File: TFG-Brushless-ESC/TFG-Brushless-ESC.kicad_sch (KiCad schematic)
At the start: 70 parts, among them J1 V, J2 USB C Receptacle, J3 HALL SENSORS, J4 SWD-I2C, J5 24V IN, J6 U, J7 W, SW1 BOOT0, SW2 NRST, U1 LM317L_SOT-89, U2 LM317, U3 STM32F411CEUx, Y1 25MHz, Y2 32.768kHz

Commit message: PCB v3
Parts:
- D8: value FERD30H100SB -> STPS30100ST; footprint Package_TO_SOT_SMD:TO-252-2 -> Package_TO_SOT_THT:TO-220-3_Vertical
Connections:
- net 24V in: now also J5.1 (Pin_1); no longer J5.2 (Pin_2)
- net GND: now also J5.2 (Pin_2); no longer J5.1 (Pin_1)
- net PA10: no longer D4.1, J3.4 (Pin_4), R15.1
- net PA8: no longer D3.1, J3.2 (Pin_2), R13.1
- net PA9: no longer D3.2, J3.3 (Pin_3), R14.1
- net PB3: now also D3.1, J3.2 (Pin_2), R13.1
- net PB4: now also D3.2, J3.3 (Pin_3), R14.1
- net PB5: now also D4.1, J3.4 (Pin_4), R15.1
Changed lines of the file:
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@@
 		)
 	)
-	(label "PB10"
+	(label "PA9"
 		(at 203.2 78.105 0)
 		(effects
@@
 		)
 	)
-	(label "PA9"
+	(label "PB4"
 		(at 232.41 128.27 0)
 		(effects
@@
 		)
 	)
-	(label "PA3"
+	(label "PA4"
 		(at 203.2 99.06 0)
 		(effects
@@
 		)
 	)
-	(label "PB0"
+	(label "PB1"
 		(at 203.2 85.725 0)
 		(effects
@@
 		)
 	)
-	(label "PA4"
+	(label "PA5"
 		(at 203.2 101.6 0)
 		(effects
@@
 		)
 	)
-	(label "PA10"
+	(label "PB5"
 		(at 232.41 125.73 0)
 		(effects
@@
 		)
 	)
-	(label "PA5"
+	(label "PA6"
 		(at 203.2 96.52 0)
 		(effects
@@
 		)
 	)
-	(label "PA6"
+	(label "PA7"
 		(at 203.2 93.98 0)
 		(effects
@@
 		)
 	)
-	(label "PB1"
+	(label "PA8"
 		(at 203.2 80.645 0)
 		(effects
@@
 		)
 	)
-	(label "PB7"
+	(label "PA3"
 		(at 203.2 109.855 0)
 		(effects
@@
 		)
 	)
-	(label "PA7"
+	(label "PB0"
 		(at 203.2 83.185 0)
 		(effects
@@
 		)
 	)
-	(label "PA8"
+	(label "PB3"
 		(at 232.41 130.81 0)
 		(effects
@@
 		)
 	)
-	(label "PB6"
+	(label "PA2"
 		(at 203.2 112.395 0)
 		(effects
@@
 	)
 	(symbol
-		(lib_id "Connector_Generic:Conn_01x02")
-		(at 56.515 184.15 180)
-		(unit 1)
-		(exclude_from_sim no)
-		(in_bom yes)
-		(on_board yes)
-		(dnp no)
-		(property "Reference" "J5"
-			(at 53.975 184.15 0)
-			(effects
-				(font
-					(size 1.27 1.27)
-				)
-				(justify left)
-			)
-		)
-		(property "Value" "24V IN"
-			(at 53.975 181.61 0)
-			(effects
-				(font
-					(size 1.27 1.27)
-				)
-				(justify left)
-			)
-		)
-		(property "Footprint" "TerminalBlock_Phoenix:TerminalBlock_Phoenix_MKDS-1,5-2-5.08_1x02_P5.08mm_Horizontal"
-			(at 56.515 184.15 0)
-			(effects
-				(font
-					(size 1.27 1.27)
-				)
-				(hide yes)
-			)
-		)
-		(property "Datasheet" "~"
-			(at 56.515 184.15 0)
-			(effects
-				(font
-					(size 1.27 1.27)
-				)
-				(hide yes)
-			)
-		)
-		(property "Description" "Generic connector, single row, 01x02, script generated (kicad-library-utils/schlib/autogen/connector/)"
-			(at 56.515 184.15 0)
-			(effects
-				(font
-					(size 1.27 1.27)
-				)
-				(hide yes)
-			)
-		)
-		(pin "2"
-		)
-		(pin "1"
-		)
-		(instances
-			(project ""
-				(path "/fc8dd9a9-f99a-4338-8182-2c8b4b8ed6dd"
-					(reference "J5")
-					(unit 1)
-				)
-			)
-		)
-	)
-	(symbol
 		(lib_id "Device:D_TVS")
 		(at 119.38 31.115 90)
@@
 	)
 	(symbol
+		(lib_id "Connector_Generic:Conn_01x02")
+		(at 56.515 181.61 0)
+		(mirror y)
+		(unit 1)
+		(exclude_from_sim no)
+		(in_bom yes)
+		(on_board yes)
+		(dnp no)
+		(property "Reference" "J5"
+			(at 53.975 181.61 0)
+			(effects
+				(font
+					(size 1.27 1.27)
+				)
+				(justify left)
+			)
+		)
+		(property "Value" "24V IN"
+			(at 53.975 184.15 0)
+			(effects
+				(font
+					(size 1.27 1.27)
+				)
+				(justify left)
+			)
+		)
+		(property "Footprint" "TerminalBlock_Phoenix:TerminalBlock_Phoenix_MKDS-1,5-2-5.08_1x02_P5.08mm_Horizontal"
+			(at 56.515 181.61 0)
+			(effects
+				(font
+					(size 1.27 1.27)
+				)
+				(hide yes)
+			)
+		)
+		(property "Datasheet" "~"
+			(at 56.515 181.61 0)
+			(effects
+				(font
+					(size 1.27 1.27)
+				)
+				(hide yes)
+			)
+		)
+		(property "Description" "Generic connector, single row, 01x02, script generated (kicad-library-utils/schlib/autogen/connector/)"
+			(at 56.515 181.61 0)
+			(effects
+				(font
+					(size 1.27 1.27)
+				)
+				(hide yes)
+			)
+		)
+		(pin "2"
+		)
+		(pin "1"
+		)
+		(instances
+			(project "TFG-Brushless-ESC"
+				(path "/fc8dd9a9-f99a-4338-8182-2c8b4b8ed6dd"
+					(reference "J5")
+					(unit 1)
+				)
+			)
+		)
+	)
+	(symbol
 		(lib_id "Device:D_Schottky_AKA")
 		(at 94.615 181.61 0)
@@
 			)
 		)
-		(property "Value" "FERD30H100SB"
+		(property "Value" "STPS30100ST"
 			(at 94.615 175.895 0)
 			(effects
@@
 			)
 		)
-		(property "Footprint" "Package_TO_SOT_SMD:TO-252-2"
+		(property "Footprint" "Package_TO_SOT_THT:TO-220-3_Vertical"
 			(at 94.615 181.61 0)
 			(effects
@@
 			)
 		)
-		(property "Datasheet" "~"
+		(property "Datasheet" "https://www.lcsc.com/datasheet/lcsc_datasheet_2410121846_Vishay-Intertech-VF30100S-E3-4W_C3759118.pdf"
 			(at 94.615 181.61 0)
 			(effects

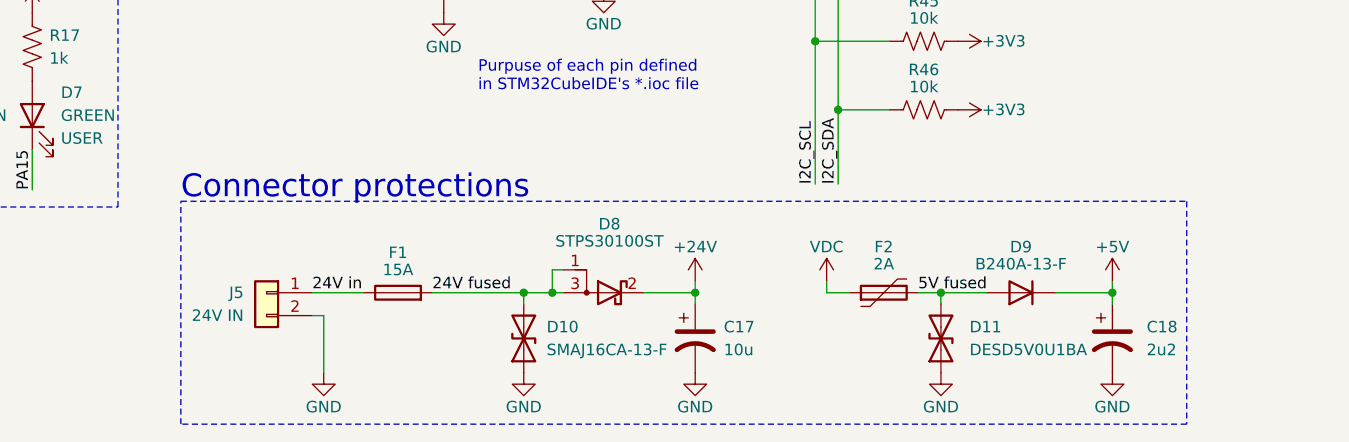
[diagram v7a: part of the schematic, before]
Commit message: updated main power connector to phoenix
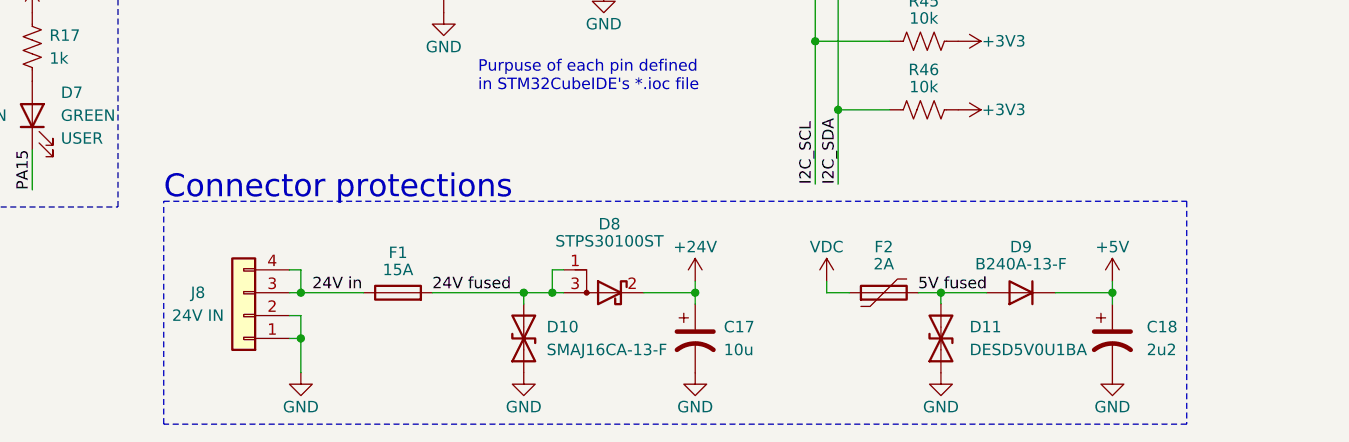
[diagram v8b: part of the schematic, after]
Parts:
- removed J5: 24V IN, TerminalBlock_Phoenix:TerminalBlock_Phoenix_MKDS-1,5-2-5.08_1x02_P5.08mm_Horizontal, symbol Connector_Generic:Conn_01x02
- added J8: 24V IN, Connector_Phoenix_MSTB:PhoenixContact_MSTBA_2,5_4-G-5,08_1x04_P5.08mm_Horizontal, symbol Connector_Generic:Conn_01x04
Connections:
- net 24V in: now also J8.3 (Pin_3), J8.4 (Pin_4)
- net GND: now also J8.1 (Pin_1), J8.2 (Pin_2)
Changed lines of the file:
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@@
 	)
 	(junction
+		(at 60.325 181.61)
+		(diameter 0)
+		(color 0 0 0 0)
+	)
+	(junction
 		(at 62.865 26.035)
 		(diameter 0)
@@
 	)
 	(junction
+		(at 60.325 186.69)
+		(diameter 0)
+		(color 0 0 0 0)
+	)
+	(junction
 		(at 34.29 122.555)
 		(diameter 0)
@@
 	(wire
 		(pts
-			(xy 62.865 184.15) (xy 62.865 190.5)
+			(xy 60.325 186.69) (xy 60.325 190.5)
 		)
 		(stroke
@@
 	(wire
 		(pts
-			(xy 61.595 184.15) (xy 62.865 184.15)
+			(xy 59.055 184.15) (xy 60.325 184.15)
 		)
 		(stroke
@@
 	(wire
 		(pts
+			(xy 60.325 186.69) (xy 60.325 184.15)
+		)
+		(stroke
+			(width 0)
+			(type default)
+		)
+	)
+	(wire
+		(pts
 			(xy 232.41 130.81) (xy 237.49 130.81)
 		)
@@
 	(wire
 		(pts
-			(xy 61.595 181.61) (xy 67.31 181.61)
+			(xy 59.055 181.61) (xy 60.325 181.61)
 		)
 		(stroke
@@
 	(wire
 		(pts
+			(xy 60.325 179.07) (xy 60.325 181.61)
+		)
+		(stroke
+			(width 0)
+			(type default)
+		)
+	)
+	(wire
+		(pts
 			(xy 237.49 130.81) (xy 237.49 136.525)
 		)
@@
 	(wire
 		(pts
+			(xy 59.055 186.69) (xy 60.325 186.69)
+		)
+		(stroke
+			(width 0)
+			(type default)
+		)
+	)
+	(wire
+		(pts
 			(xy 95.25 26.035) (xy 95.25 27.305)
 		)
@@
 	(wire
 		(pts
+			(xy 60.325 181.61) (xy 67.31 181.61)
+		)
+		(stroke
+			(width 0)
+			(type default)
+		)
+	)
+	(wire
+		(pts
 			(xy 164.465 36.195) (xy 164.465 33.655)
 		)
@@
 	(wire
 		(pts
+			(xy 59.055 179.07) (xy 60.325 179.07)
+		)
+		(stroke
+			(width 0)
+			(type default)
+		)
+	)
+	(wire
+		(pts
 			(xy 236.22 34.925) (xy 236.22 36.195)
 		)
@@
 	)
 	(rectangle
-		(start 46.99 171.45)
+		(start 45.085 171.45)
 		(end 158.75 196.215)
 		(stroke
@@
 	(text "Connector protections"
 		(exclude_from_sim no)
-		(at 46.99 171.45 0)
+		(at 45.085 171.45 0)
 		(effects
 			(font
@@
 	)
 	(symbol
+		(lib_id "Connector_Generic:Conn_01x04")
+		(at 53.975 184.15 180)
+		(unit 1)
+		(exclude_from_sim no)
+		(in_bom yes)
+		(on_board yes)
+		(dnp no)
+		(property "Reference" "J8"
+			(at 48.895 181.61 0)
+			(effects
+				(font
+					(size 1.27 1.27)
+				)
+			)
+		)
+		(property "Value" "24V IN"
+			(at 48.895 184.15 0)
+			(effects
+				(font
+					(size 1.27 1.27)
+				)
+			)
+		)
+		(property "Footprint" "Connector_Phoenix_MSTB:PhoenixContact_MSTBA_2,5_4-G-5,08_1x04_P5.08mm_Horizontal"
+			(at 53.975 184.15 0)
+			(effects
+				(font
+					(size 1.27 1.27)
+				)
+				(hide yes)
+			)
+		)
+		(property "Datasheet" "https://www.lcsc.com/datasheet/lcsc_datasheet_2408130957_Ningbo-Kangnex-Elec-WJ2EDGRC-5-08-4P_C8446.pdf"
+			(at 53.975 184.15 0)
+			(effects
+				(font
+					(size 1.27 1.27)
+				)
+				(hide yes)
+			)
+		)
+		(property "Description" "C8446"
+			(at 53.975 184.15 0)
+			(effects
+				(font
+					(size 1.27 1.27)
+				)
+				(hide yes)
+			)
+		)
+		(pin "1"
+		)
+		(pin "3"
+		)
+		(pin "2"
+		)
+		(pin "4"
+		)
+		(instances
+			(project ""
+				(path "/fc8dd9a9-f99a-4338-8182-2c8b4b8ed6dd"
+					(reference "J8")
+					(unit 1)
+				)
+			)
+		)
+	)
+	(symbol
 		(lib_id "Device:R_US")
 		(at 95.25 31.115 0)
@@
 	(symbol
 		(lib_id "power:GND")
-		(at 62.865 190.5 0)
+		(at 60.325 190.5 0)
 		(mirror y)
 		(unit 1)
@@
 		(dnp no)
 		(property "Reference" "#PWR054"
-			(at 62.865 196.85 0)
+			(at 60.325 196.85 0)
 			(effects
 				(font
@@
 		)
 		(property "Value" "GND"
-			(at 62.865 194.31 0)
+			(at 60.325 194.31 0)
 			(effects
 				(font
@@
 		)
 		(property "Footprint" ""
-			(at 62.865 190.5 0)
+			(at 60.325 190.5 0)
 			(effects
 				(font
@@
 		)
 		(property "Datasheet" ""
-			(at 62.865 190.5 0)
+			(at 60.325 190.5 0)
 			(effects
 				(font
@@
 		)
 		(property "Description" ""
-			(at 62.865 190.5 0)
+			(at 60.325 190.5 0)
 			(effects
 				(font
@@
 					(unit 1)
 				)
-			)
-		)
-	)
-	(symbol
-		(lib_id "Connector_Generic:Conn_01x02")
-		(at 56.515 181.61 0)
-		(mirror y)
-		(unit 1)
-		(exclude_from_sim no)
-		(in_bom yes)
-		(on_board yes)
-		(dnp no)
-		(property "Reference" "J5"
-			(at 53.975 181.61 0)
-			(effects
-				(font
-					(size 1.27 1.27)
-				)
-				(justify left)
-			)
-		)
-		(property "Value" "24V IN"
-			(at 53.975 184.15 0)
-			(effects
-				(font
-					(size 1.27 1.27)
-				)
-				(justify left)
-			)
-		)
-		(property "Footprint" "TerminalBlock_Phoenix:TerminalBlock_Phoenix_MKDS-1,5-2-5.08_1x02_P5.08mm_Horizontal"
-			(at 56.515 181.61 0)
-			(effects
-				(font
-					(size 1.27 1.27)
-				)
-				(hide yes)
-			)
-		)
-		(property "Datasheet" "~"
-			(at 56.515 181.61 0)
-			(effects
-				(font
-					(size 1.27 1.27)
-				)
-				(hide yes)
-			)
-		)
-		(property "Description" "Generic connector, single row, 01x02, script generated (kicad-library-utils/schlib/autogen/connector/)"
-			(at 56.515 181.61 0)
-			(effects
-				(font
-					(size 1.27 1.27)
-				)
-				(hide yes)
-			)
-		)
-		(pin "2"
-		)
-		(pin "1"
-		)
-		(instances
-			(project "TFG-Brushless-ESC"
-				(path "/fc8dd9a9-f99a-4338-8182-2c8b4b8ed6dd"
-					(reference "J5")
-					(unit 1)
-				)
